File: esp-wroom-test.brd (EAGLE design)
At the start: 35.7 x 27.4 mm, 15 parts, among them U8 NCP1117LPST50T3G

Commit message: as ordered
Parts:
- removed CONN2: STEMMA_I2C_QT, 00jim:JST_SH4
- removed R2: (no value), 00jim:R0603
- added -_+_G_V_T_R_E_1: MF-CON-2.54mm-01x08, SparkFun-Connectors:1X08
- added C4: 10uF, SparkFun-Capacitors:EIA3216
- added D2: BAS16, SparkFun-DiscreteSemi:SOD-323
- added IC1: TCAN1051HGV, microbuilder:SOIC8_150MIL
- added JP1: DB9, SparkFun-Connectors:DB9
- added POW3: (no value), MF_Passives:C1206
- added R10, R11: 10K, SparkFun-Resistors:0603-RES
- added R8: 200, 00jim:R0603
- added U1: NCP1117LPST50T3G, MF_IC_Power:SOT-223-3
- added U2: XN04312, SparkFun-DiscreteSemi:SOT23-6
- POW1, POW2: device MF_Passives:C1210 -> MF_Passives:C1206
- moved R3 28.7 mm to (34.5, 24.4)
- moved R5 11.5 mm to (13.0, 25.4)
- moved R4 6.48 mm to (9.91, 25.4)
- moved U$3 3.81 mm to (36.8, 19.6)
- moved R1 1.80 mm to (29.5, 24.4)
- moved R7 1.55 mm to (32.0, 24.4)
- moved R6 1.27 mm to (15.5, 25.4)
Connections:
- removed net IO0: -_+_G_V_T_R_E_0.8
- removed net IO12: U$3.IO12
- removed net IO15: U$3.IO15
- removed net PD: R2.P$1
- removed net VCC1: D1.A, R1.P$2, R3.P$2, R4.P$2, R6.P$2
- new net CANRX: IC1.4, U$3.IO18
- new net CANTX: IC1.1, U$3.IO19
- new net CAN_H: IC1.7, JP1.1, R8.P$1
- new net CAN_L: IC1.6, JP1.2, R8.P$2
- new net CAN_S: IC1.8, U$3.IO17
- new net DB9_RX: U$3.IO26, U2.2
- new net DB9_TX: R11.1, U$3.IO27, U2.1
- new net N$4: C4.C, D2.A, R10.1
- new net RS-IN: D2.C, JP1.5, U2.5
- new net RS-OUT: JP1.4, R10.2, U2.4
- new net UNITID: -_+_G_V_T_R_E_0.1, -_+_G_V_T_R_E_1.1, JP1.3
- new net VCC_50: IC1.3, POW3.P$1, U1.P$1, U1.P$3
- net EN: now also -_+_G_V_T_R_E_1.7
- net GND: now also -_+_G_V_T_R_E_1.3, C4.A, IC1.2, JP1.6, JP1.9, POW3.P$2, U1.P$2, U2.6; no longer -_+_G_V_T_R_E_0.1, CONN2.1, R2.P$2
- net IO00: now also -_+_G_V_T_R_E_0.8, -_+_G_V_T_R_E_1.8
- net RAW: now also -_+_G_V_T_R_E_1.2, JP1.7, JP1.8, U1.P$4
- net RXI: now also -_+_G_V_T_R_E_1.6
- net SCL: no longer CONN2.4
- net SDA: no longer CONN2.3
- net TXO: now also -_+_G_V_T_R_E_1.5
- net VCC: now also -_+_G_V_T_R_E_1.4, D1.A, IC1.5, R1.P$2, R11.2, R3.P$2, R4.P$2, R6.P$2, U2.3; no longer CONN2.2
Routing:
- net VCC: track 68.6 -> 149.8 mm, vias 1 -> 7
- net RAW: track 6.76 -> 86.9 mm, vias 0 -> 1
- net UNITID: track 0.00 -> 77.5 mm, vias 0 -> 2
- net GND: track 100.4 -> 172.0 mm, vias 1 -> 4
- net TXO: track 15.9 -> 67.0 mm, vias 0 -> 1
- net VCC_50: track 0.00 -> 47.7 mm, vias 0 -> 2
- net RXI: track 17.4 -> 63.1 mm, vias 1 -> 0
- net CAN_H: track 0.00 -> 43.2 mm, vias 0 -> 4
- net CAN_S: track 0.00 -> 42.2 mm, vias 0 -> 2
- net IO00: track 18.8 -> 60.0 mm, vias 0 -> 3
- net CAN_L: track 0.00 -> 39.6 mm, vias 0 -> 2
- net CANTX: track 0.00 -> 36.1 mm
- net VCC1: track 32.1 -> 0.00 mm
- net CANRX: track 0.00 -> 31.6 mm, vias 0 -> 2
- net EN: track 42.3 -> 73.8 mm, vias 1 -> 2
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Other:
- board size 35.7 x 27.4 mm -> 44.4 x 38.9 mm

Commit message: Ordered again
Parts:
- added CONN1: STEMMA_I2C_QT, 01jim:JST_SH4
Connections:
- net GND: now also CONN1.1
- net IO00: no longer -_+_G_V_T_R_E_0.8, -_+_G_V_T_R_E_1.8
- net SCL: now also CONN1.4
- net SDA: now also CONN1.3
- net VCC: now also CONN1.2
- net VCC_50: now also -_+_G_V_T_R_E_0.8, -_+_G_V_T_R_E_1.8
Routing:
- net IO00: track 60.0 -> 14.0 mm, vias 3 -> 0
- net VCC_50: track 47.7 -> 69.2 mm, vias 2 -> 3
- net IO14: track 27.2 -> 40.7 mm, vias 4 -> 2
- net RAW: track 86.9 -> 76.3 mm, vias 1 -> 2
- net RXI: track 63.1 -> 54.0 mm, vias 0 -> 1
- net TXO: track 67.0 -> 58.3 mm, vias 1 -> 2
- net DB9_TX: track 29.0 -> 37.2 mm, vias 2 -> 5
- net GND: track 172.0 -> 177.1 mm, vias 4 -> 3
- net CAN_H: track 43.2 -> 38.3 mm, vias 4 -> 2
- net SCL: track 55.7 -> 51.7 mm, vias 4 -> 6
- net VCC: track 149.8 -> 153.1 mm
- net EN: track 73.8 -> 72.5 mm, vias 2 -> 4
- net CANTX: track 36.1 -> 34.8 mm
- net N$4: track 11.8 -> 10.7 mm
- net CANRX: track 31.6 -> 32.6 mm
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
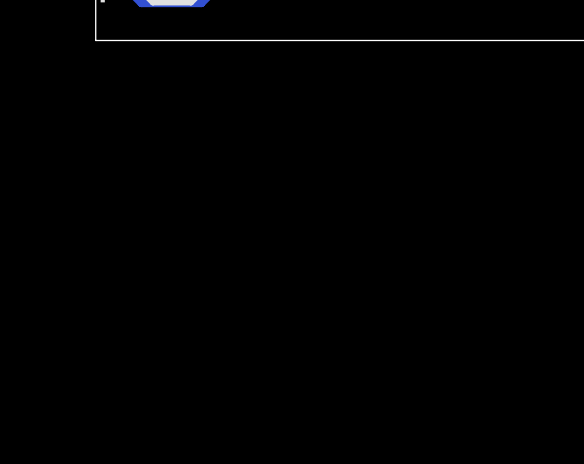
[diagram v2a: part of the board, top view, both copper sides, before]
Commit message: Narrow board, add esp32 reset mechanism
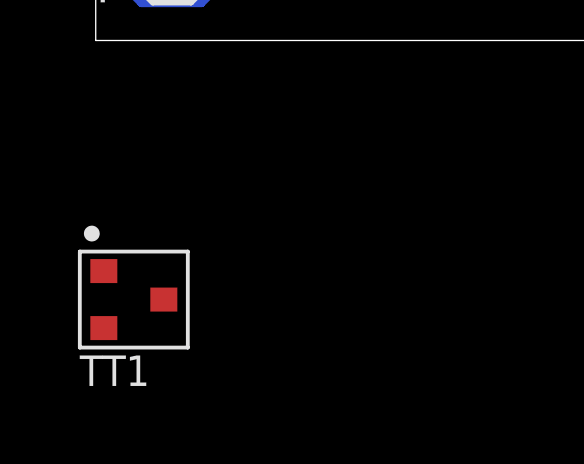
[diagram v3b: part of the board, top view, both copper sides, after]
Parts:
- added TT1: MF-DSC-SOT233-MMBT3904, MF_Discrete_Semiconductor:SOT-23-3
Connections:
- new net IO21_D1: TT1.P$3
- new net N$1: TT1.P$2
- new net N$3: TT1.P$1
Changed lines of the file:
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@@
 <attribute name="NAME" x="7.17" y="31.016" size="1.778" layer="25" rot="R270"/>
+</element>
+<element name="TT1" library="MF_Discrete_Semiconductor" package="SOT-23-3" value="MF-DSC-SOT233-MMBT3904" x="1.27" y="-8.636" smashed="yes">
+<attribute name="HOUSEPART" value="YES" x="-4.318" y="-2.54" size="1.778" layer="27" display="off"/>
+<attribute name="MPN" value="MF-DSC-SOT233-MMBT3904" x="-4.318" y="-2.54" size="1.778" layer="27" display="off"/>
+<attribute name="NAME" x="-0.53" y="-11.516" size="1.016" layer="25" font="vector" ratio="16"/>
+<attribute name="POPULATE" value="1" x="-4.318" y="-2.54" size="1.778" layer="27" display="off"/>
+<attribute name="URL" value="https://factory.macrofab.com/part/MF-DSC-SOT233-MMBT3904" x="-4.318" y="-2.54" size="1.778" layer="27" display="off"/>
 </element>
 </elements>
@@
 <via x="15.24" y="27.71775" extent="1-16" drill="0.35"/>
 </signal>
+<signal name="IO21_D1">
+<contactref element="TT1" pad="P$3"/>
+</signal>
+<signal name="N$1">
+<contactref element="TT1" pad="P$2"/>
+</signal>
+<signal name="N$3">
+<contactref element="TT1" pad="P$1"/>
+</signal>
 </signals>

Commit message: Actually save
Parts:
- removed CONN1: STEMMA_I2C_QT, 01jim:JST_SH4
- removed R3, R6: (no value), 00jim:R0603
- removed R8: 200, 00jim:R0603
- added R12, R13, R2, R9: (no value), 00jim:R0603
- added TT2: MF-DSC-SOT233-MMBT3904, MF_Discrete_Semiconductor:SOT-23-3
- moved U$3 33.3 mm to (7.37, 4.06), turned to 270 degrees
- moved TT1 28.3 mm to (3.56, 19.6)
- moved R1 26.7 mm to (2.79, 25.1)
- moved R7 23.4 mm to (8.64, 25.1)
- moved -_+_G_V_T_R_E_0 16.5 mm to (2.54, -14.0)
- moved IC1 16.4 mm to (22.9, 24.4), turned to 90 degrees
- moved U8 16.3 mm to (24.9, 10.7)
- moved -_+_G_V_T_R_E_1 12.9 mm to (31.0, 30.0)
- moved POW1 12.5 mm to (18.5, 10.4), turned to 90 degrees
- moved U2 10.9 mm to (19.6, 29.2)
- moved R11 8.89 mm to (15.2, 29.2), turned to 90 degrees
- moved R10 8.13 mm to (12.2, 29.2), turned to 90 degrees
- moved U1 8.12 mm to (6.10, 10.2)
- moved C4 7.37 mm to (7.87, 29.0)
- moved D2 7.12 mm to (3.05, 29.0)
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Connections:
- removed net IO21_D1: TT1.P$3
- removed net N$1: TT1.P$2
- new net DTR: -_+_G_V_T_R_E_0.7, -_+_G_V_T_R_E_1.7, R9.P$1, TT1.P$2
- new net N$6: R9.P$2, TT2.P$1
- new net RTS: -_+_G_V_T_R_E_0.8, -_+_G_V_T_R_E_1.8, R2.P$1, TT2.P$2
- new net RXI_P: -_+_G_V_T_R_E_0.6, -_+_G_V_T_R_E_1.6, R13.P$1
- new net TXO_P: -_+_G_V_T_R_E_0.5, -_+_G_V_T_R_E_1.5, R12.P$1
- net CAN_H: no longer R8.P$1
- net CAN_L: no longer R8.P$2
- net EN: now also TT2.P$3; no longer -_+_G_V_T_R_E_0.7, -_+_G_V_T_R_E_1.7
- net GND: no longer CONN1.1
- net IO00: now also TT1.P$3
- net N$3: now also R2.P$2
- net RXI: now also R13.P$2; no longer -_+_G_V_T_R_E_0.6, -_+_G_V_T_R_E_1.6
- net SCL: no longer CONN1.4, R3.P$1
- net SDA: no longer CONN1.3, R6.P$1
- net TXO: now also R12.P$2; no longer -_+_G_V_T_R_E_0.5, -_+_G_V_T_R_E_1.5
- net VCC: no longer CONN1.2, R3.P$2, R6.P$2
- net VCC_50: no longer -_+_G_V_T_R_E_0.8, -_+_G_V_T_R_E_1.8
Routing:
- net DTR: track 0.00 -> 65.7 mm, vias 0 -> 3
- net RTS: track 0.00 -> 60.7 mm, vias 0 -> 1
- net IO00: track 14.0 -> 71.2 mm, vias 0 -> 2
- net TXO_P: track 0.00 -> 53.7 mm, vias 0 -> 2
- net SCL: track 51.7 -> 0.00 mm, vias 6 -> 0
- net RXI_P: track 0.00 -> 47.5 mm, vias 0 -> 1
- net VCC: track 153.1 -> 117.4 mm, vias 7 -> 5
- net SDA: track 34.0 -> 0.00 mm, vias 2 -> 0
- net EN: track 72.5 -> 40.0 mm
- net IO02: track 12.3 -> 41.3 mm, vias 0 -> 4
- net CAN_L: track 40.5 -> 11.9 mm, vias 3 -> 1
- net VCC_50: track 69.2 -> 41.7 mm, vias 3 -> 5
- net CAN_H: track 38.3 -> 14.2 mm, vias 2 -> 1
- net RAW: track 76.3 -> 96.8 mm
- net IO14: track 40.7 -> 22.0 mm, vias 2 -> 0
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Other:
- board size 44.4 x 38.9 mm -> 32.9 x 55.4 mm

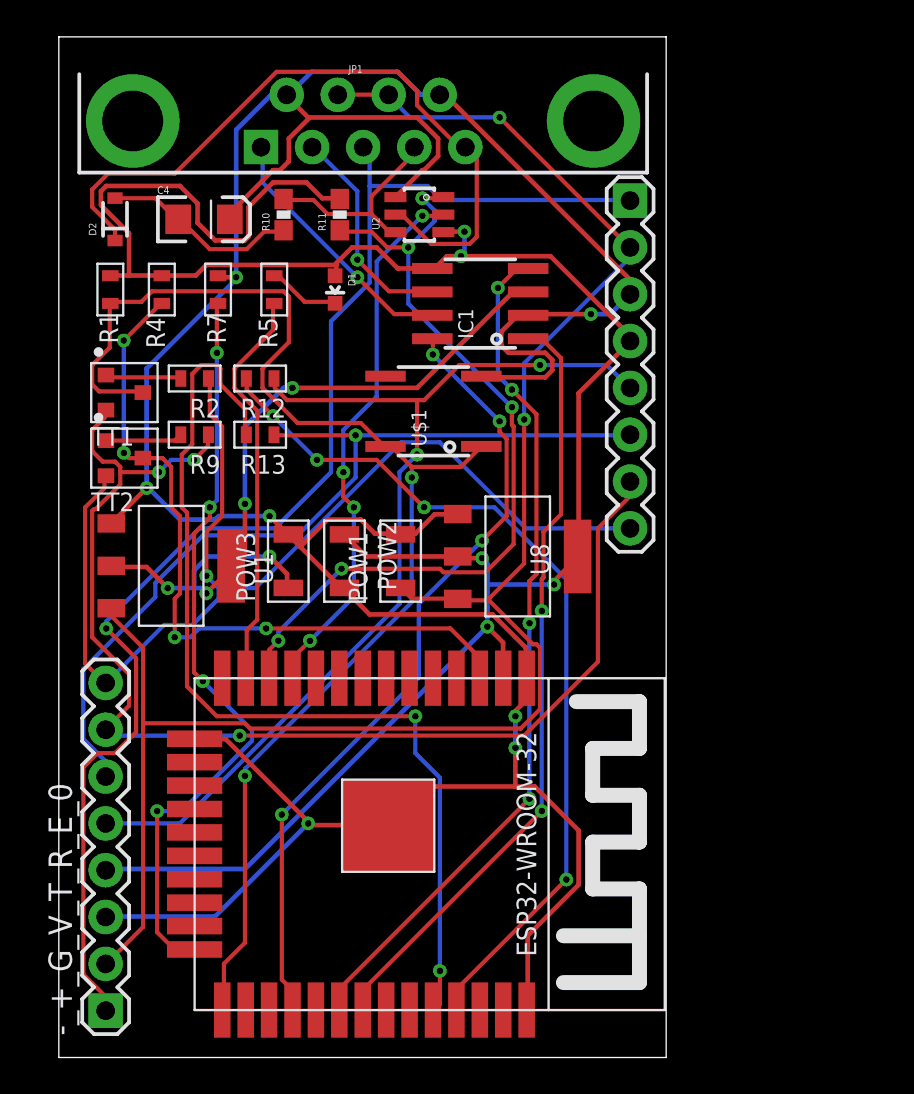
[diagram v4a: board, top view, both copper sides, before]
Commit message: wroom test two sided
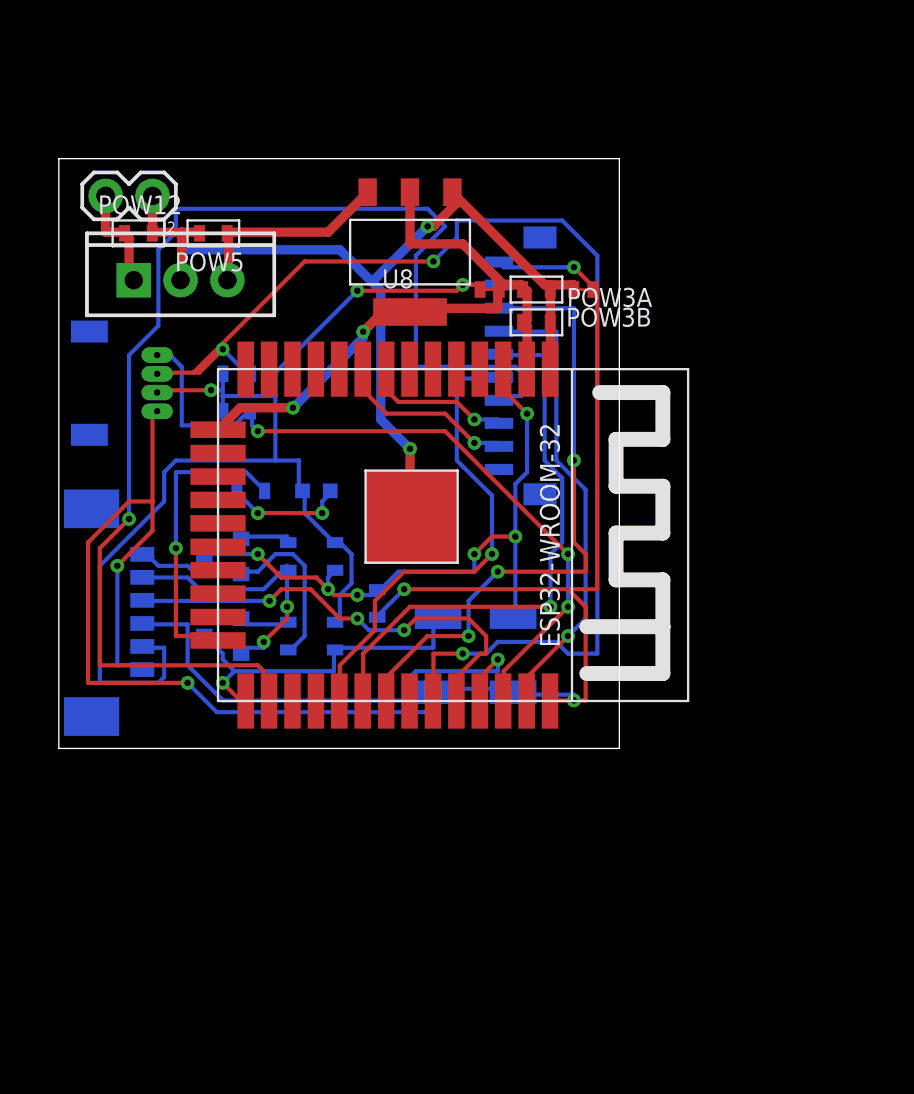
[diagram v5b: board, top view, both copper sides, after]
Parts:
- removed -_+_G_V_T_R_E_0, -_+_G_V_T_R_E_1: MF-CON-2.54mm-01x08, SparkFun-Connectors:1X08
- removed C4: 10uF, SparkFun-Capacitors:EIA3216
- removed D2: BAS16, SparkFun-DiscreteSemi:SOD-323
- removed IC1: TCAN1051HGV, microbuilder:SOIC8_150MIL
- removed JP1: DB9, SparkFun-Connectors:DB9
- removed POW1, POW2, POW3: (no value), MF_Passives:C1206
- removed R1, R12, R13, R7: (no value), 00jim:R0603
- removed R10, R11: 10K, SparkFun-Resistors:0603-RES
- removed U1: NCP1117LPST50T3G, MF_IC_Power:SOT-223-3
- removed U2: XN04312, SparkFun-DiscreteSemi:SOT23-6
- added CEN, POW12, POW3A, POW3B, POW5: (no value), MF_Passives:C0603
- added J1: (no value), 00jim:1X6-1.25MM-SMD
- added J2: (no value), SparkFun-Connectors:1X02
- added J3: (no value), SparkFun-Connectors:1X10-1.25MM
- added J4: Vertical Qwiic Connector, 00jim:JST04_1MM_HOLES
- added RCAN1, RCAN2, REN, RGP00, RLED: (no value), 00jim:R0603
- added U$2: AMAZON_BUTTONB2010, 00jim:C2010
- added U3: (no value), SparkFun-IC-Power:TO220-IGO
- R4, R5: device 00jim:R0603 -> 00jim:R0603_JMP
- U$1: value AMAZON_BUTTON -> AMAZON_BUTTONB2010; device 00jim:AMAZON_BUTTON -> 00jim:C2010
- moved R4 22.9 mm to (28.4, 25.1), turned to 180 degrees
- moved U8 17.5 mm to (19.1, 27.2), turned to 270 degrees
- moved U$3 16.8 mm to (8.64, 20.8)
- moved R2 14.9 mm to (12.4, 6.35), flipped to the bottom, turned to 90 degrees
- moved TT1 14.2 mm to (8.89, 6.35), flipped to the bottom
- moved U$1 13.2 mm to (20.6, 5.33), flipped to the bottom, turned to 270 degrees
- moved R5 11.7 mm to (23.4, 25.1), turned to 0 degrees
- moved D1 11.0 mm to (14.0, 14.2), flipped to the bottom, turned to 90 degrees
- moved R9 8.33 mm to (12.4, 10.7), flipped to the bottom, turned to 90 degrees
- moved TT2 7.54 mm to (8.89, 10.7), flipped to the bottom
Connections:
- removed net CAN_H: IC1.7, JP1.1
- removed net CAN_L: IC1.6, JP1.2
- removed net IO02: R7.P$1, U$3.IO2
- removed net IO14: R5.P$1, U$3.IO14
- removed net N$4: C4.C, D2.A, R10.1
- removed net RS-IN: D2.C, JP1.5, U2.5
- removed net RS-OUT: JP1.4, R10.2, U2.4
- removed net RXI_P: -_+_G_V_T_R_E_0.6, -_+_G_V_T_R_E_1.6, R13.P$1
- removed net SCL: U$3.IO22
- removed net SDA: U$3.IO21
- removed net TXO_P: -_+_G_V_T_R_E_0.5, -_+_G_V_T_R_E_1.5, R12.P$1
- removed net UNITID: -_+_G_V_T_R_E_0.1, -_+_G_V_T_R_E_1.1, JP1.3
- new net BUZZ: U$3.IO14
- new net GND_HC: J2.1, POW12.P$2, POW3A.P$2, POW3B.P$2, POW5.P$2, R4.P$1, U$3.GND1, U$3.GND4, U3.GND, U8.P$2
- new net GPS_RX: U$3.SENSOR_VP
- new net GPS_TX: U$3.IO12
- new net LED: RLED.P$1, U$3.IO2
- new net MISO: J3.3, U$3.IO19
- new net MOSI: J3.4, U$3.IO23
- new net RX2: U$3.SENSOR_VN
- new net RX3: U$3.IO34
- new net SCL1: J4.P$4, RCAN2.P$1, U$3.IO22
- new net SCLK: J3.5, U$3.IO18
- new net SDA1: J4.P$3, RCAN1.P$1, U$3.IO21
- new net SWITCH: U$3.IO35
- new net TCH_CS: J3.7, U$3.IO4
- new net TFT_CS: J3.6, U$3.IO5
- new net TFT_DC: J3.8, U$3.IO32
- new net TFT_RST: J3.9, U$3.IO33
- new net TX2: U$3.IO25
- new net TX3: U$3.IO13
- new net VCC_HC: POW3A.P$1, POW3B.P$1, R5.P$1, U$3.3V3, U$3.GND2, U8.P$1, U8.P$3
- net CANRX: now also U$3.IO16; no longer IC1.4, U$3.IO18
- net CANTX: now also U$3.IO15; no longer IC1.1, U$3.IO19
- net CAN_S: no longer IC1.8
- net DB9_RX: no longer U2.2
- net DB9_TX: no longer R11.1, U2.1
- net DTR: now also J1.5; no longer -_+_G_V_T_R_E_0.7, -_+_G_V_T_R_E_1.7
- net EN: now also CEN.P$1, REN.P$1, U$2.P$1; no longer R4.P$1
- net GND: now also CEN.P$2, J1.1, J3.1, J4.P$1, R4.P$2, U$1.P$2, U$2.P$2; no longer -_+_G_V_T_R_E_0.3, -_+_G_V_T_R_E_1.3, C4.A, IC1.2, JP1.6, JP1.9, POW1.P$2, POW2.P$2, POW3.P$2, R7.P$2, U$1.2, U$1.3, U$3.GND1, U$3.GND2, U$3.GND4, U1.P$2, U2.6, U8.P$2
- net IO00: now also RGP00.P$1, U$1.P$1; no longer R1.P$1, U$1.1, U$1.4
- net N$2: now also RLED.P$2; no longer R5.P$2
- net RAW: now also J2.2, POW12.P$1, U3.IN; no longer -_+_G_V_T_R_E_0.2, -_+_G_V_T_R_E_1.2, JP1.7, JP1.8, POW1.P$1, U1.P$4, U8.P$4
- net RTS: now also J1.6; no longer -_+_G_V_T_R_E_0.8, -_+_G_V_T_R_E_1.8
- net RXI: now also J1.4; no longer R13.P$2
- net TXO: now also J1.3; no longer R12.P$2
- net VCC: now also J1.2, J3.2, J4.P$2, R5.P$2, RCAN1.P$2, RCAN2.P$2, REN.P$2, RGP00.P$2; no longer -_+_G_V_T_R_E_0.4, -_+_G_V_T_R_E_1.4, IC1.5, POW2.P$1, R1.P$2, R11.2, R4.P$2, U$3.3V3, U2.3, U8.P$1, U8.P$3
- net VCC_50: now also POW5.P$1, U3.OUT, U8.P$4; no longer IC1.3, POW3.P$1, U1.P$1, U1.P$3
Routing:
- net RAW: track 96.8 -> 5.85 mm, vias 2 -> 0
- net GND: track 181.4 -> 100.1 mm, vias 7 -> 5
- net UNITID: track 72.7 -> 0.00 mm, vias 1 -> 0
- net TCH_CS: track 0.00 -> 69.1 mm, vias 0 -> 1
- net SDA1: track 0.00 -> 66.4 mm, vias 0 -> 3
- net GND_HC: track 0.00 -> 54.1 mm, vias 0 -> 2
- net TXO_P: track 53.7 -> 0.00 mm, vias 2 -> 0
- net IO00: track 71.2 -> 18.9 mm, vias 2 -> 1
- net VCC: track 117.4 -> 66.0 mm, vias 5 -> 3
- net DTR: track 65.7 -> 15.0 mm, vias 3 -> 2
- net RXI_P: track 47.5 -> 0.00 mm, vias 1 -> 0
- net CANRX: track 46.6 -> 0.00 mm, vias 4 -> 0
- net RTS: track 60.7 -> 15.0 mm, vias 1 -> 0
- net DB9_TX: track 44.9 -> 0.00 mm, vias 5 -> 0
- net CAN_S: track 43.4 -> 0.00 mm, vias 4 -> 0
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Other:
- board size 32.9 x 55.4 mm -> 30.4 x 32 mm

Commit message: Change wroom test to 12-06 resistors/leds
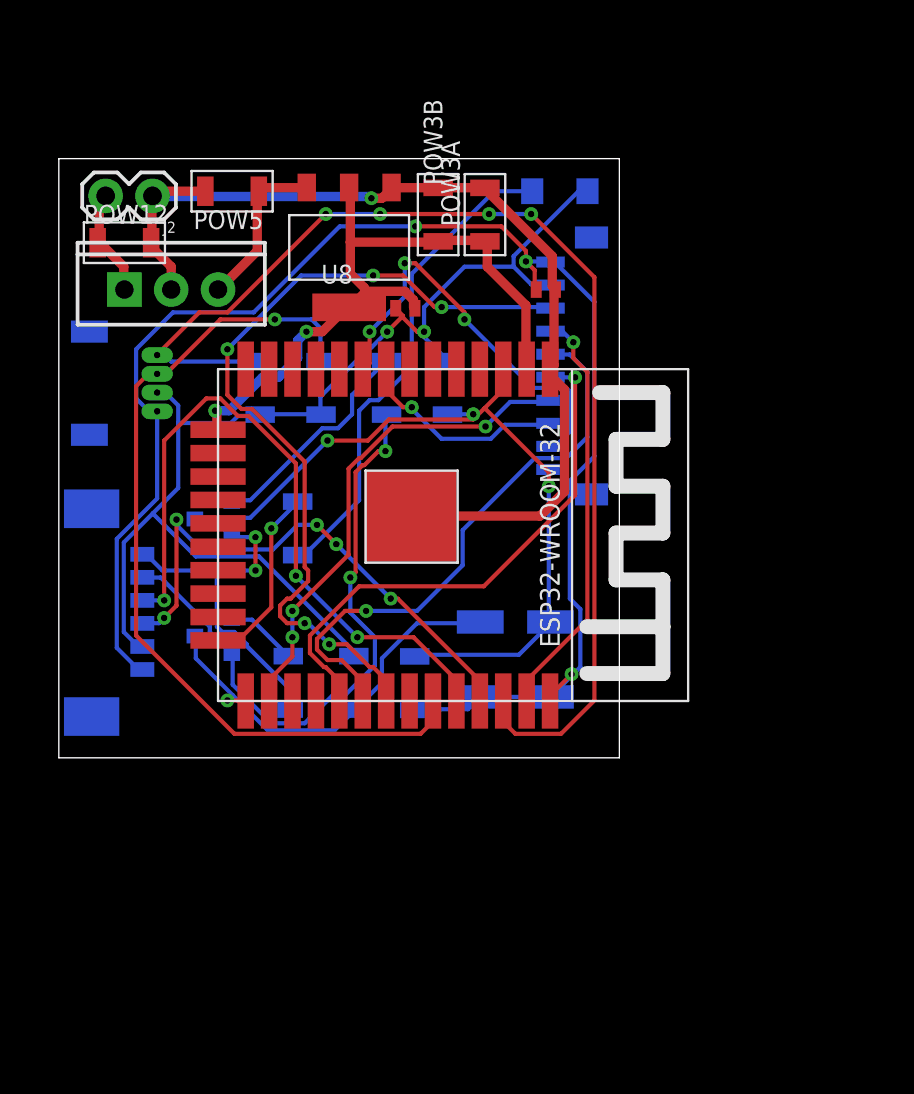
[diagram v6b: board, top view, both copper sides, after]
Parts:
- removed RCAN1, RCAN2: (no value), 00jim:R0603
- removed U$1, U$2: AMAZON_BUTTONB2010, 00jim:C2010
- added PU1, PU2: (no value), 00jim:R1206
- added SW1, SW2: AMAZON_BUTTONB2010, 00jim:C2010
- CEN, POW12, POW3A, POW3B, POW5: device MF_Passives:C0603 -> MF_Passives:C1206
- D1: device 00jim:LED-0603 -> 00jim:LED-1206
- R2, R9, REN, RGP00, RLED: device 00jim:R0603 -> 00jim:R1206
- moved D1 20.9 mm to (27.2, 30.5), turned to 0 degrees
- moved REN 11.0 mm to (21.1, 19.8)
- moved R9 10.6 mm to (17.8, 19.8)
- moved POW3B 7.91 mm to (20.6, 29.2), turned to 90 degrees
- moved POW3A 4.93 mm to (23.1, 29.2), turned to 90 degrees
- moved CEN 4.77 mm to (19.3, 3.80)
- moved R5 4.68 mm to (18.8, 24.1)
- moved U8 3.31 mm to (15.7, 27.4)
- moved RLED 3.25 mm to (13.0, 12.2), turned to 270 degrees
- moved J3 2.79 mm to (29.2, 22.9)
- moved RGP00 2.74 mm to (16.0, 3.81)
- moved R2 2.54 mm to (12.4, 3.81)
- moved POW5 2.50 mm to (9.40, 30.5)
- moved TT2 2.09 mm to (8.38, 12.7)
- moved R4 2.03 mm to (26.4, 25.1), turned to 0 degrees
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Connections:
- net EN: now also SW1.P$1; no longer U$2.P$1
- net GND: now also SW1.P$2, SW2.P$2; no longer U$1.P$2, U$2.P$2
- net IO00: now also SW2.P$1; no longer U$1.P$1
- net SCL1: now also PU2.P$1; no longer RCAN2.P$1
- net SDA1: now also PU1.P$1; no longer RCAN1.P$1
- net VCC: now also PU1.P$2, PU2.P$2; no longer RCAN1.P$2, RCAN2.P$2
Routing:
- net TCH_CS: track 69.1 -> 26.9 mm, vias 1 -> 3
- net SCL1: track 39.0 -> 64.2 mm, vias 3 -> 4
- net N$2: track 6.51 -> 26.7 mm, vias 2 -> 0
- net SDA1: track 66.4 -> 46.7 mm, vias 3 -> 1
- net DTR: track 15.0 -> 33.6 mm
- net GND: track 100.1 -> 83.7 mm, vias 5 -> 3
- net RXI: track 24.9 -> 37.7 mm
- net TFT_RST: track 9.83 -> 22.4 mm, vias 1 -> 3
- net MISO: track 34.2 -> 45.6 mm, vias 3 -> 5
- net N$6: track 2.90 -> 12.2 mm
- net EN: track 35.3 -> 43.7 mm, vias 6 -> 3
- net LED: track 16.6 -> 9.98 mm
- net RTS: track 15.0 -> 19.2 mm, vias 0 -> 2
- net IO00: track 18.9 -> 23.0 mm
- net TFT_DC: track 8.05 -> 11.6 mm
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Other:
- board size 30.4 x 32 mm -> 30.4 x 32.5 mm
